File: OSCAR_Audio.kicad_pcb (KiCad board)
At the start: 2 copper layers, 91 x 87.1 mm, 125 parts, among them J1 InL, J2 InR, J3 OutR, J4 OutL, J5 SAI, J6 Vol, J7 +12V, J8 +12V, J9 ByPass, K1 G6K-2F-Y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

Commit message: Fix typo OPA1612 -> OPA1642. Note: an OPA with FET inputs is necessary here.
/!\  An OPA with FET inputs is necessary here.
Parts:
- U1: value OPA1612 -> OPA1642
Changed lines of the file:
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@@
 			)
 		)
-		(property "Value" "OPA1612"
-			(at -1.4525 4.085 0)
+		(property "Value" "OPA1642"
+			(at -1.2825 4.845 0)
 			(layer "B.SilkS")
 			(effects

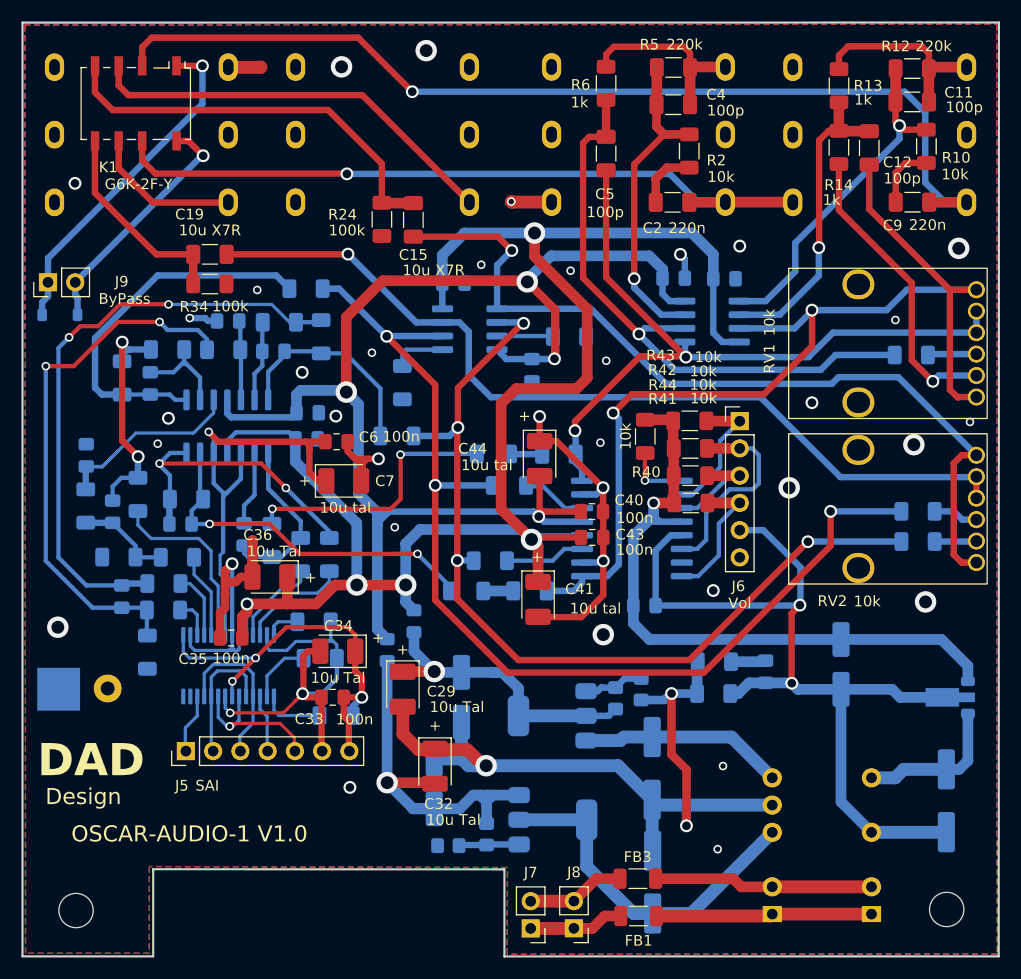
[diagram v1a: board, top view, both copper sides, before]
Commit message: Invert output summing stage to maintain correct phase
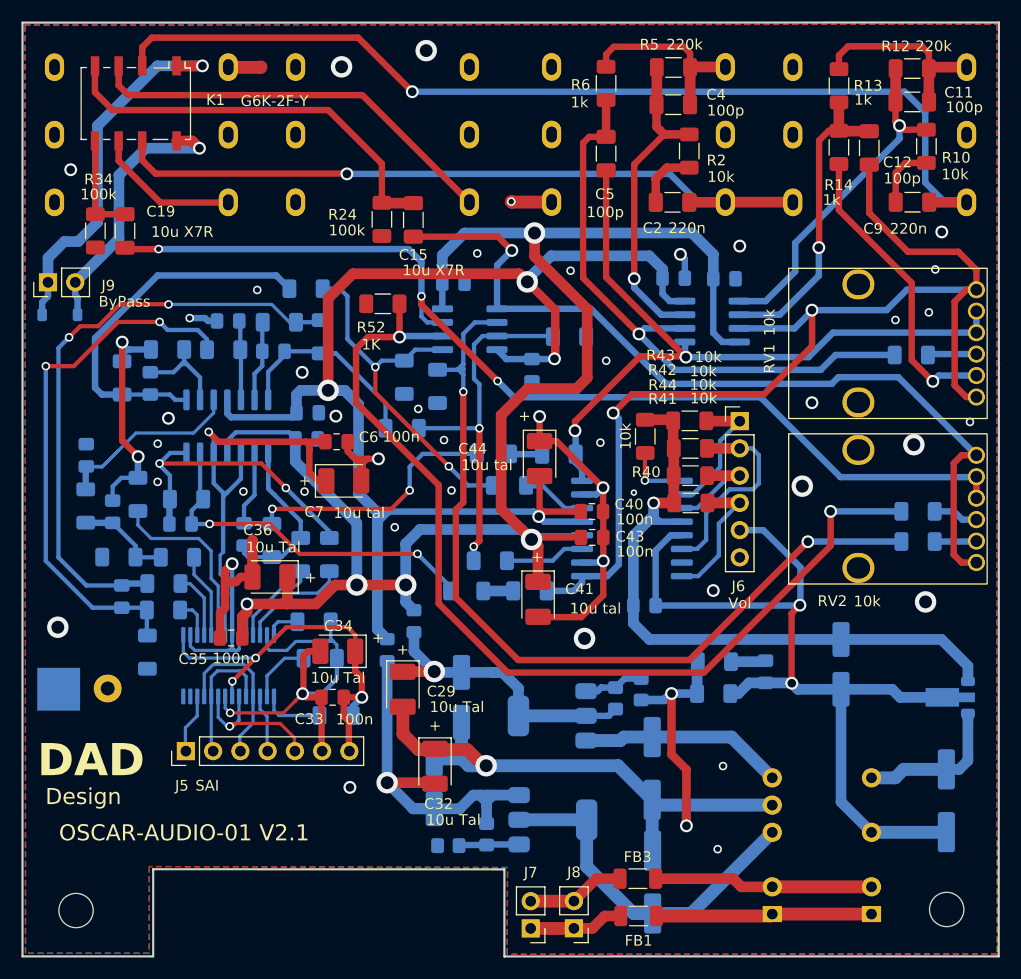
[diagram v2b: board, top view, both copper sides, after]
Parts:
- added R51: 1k, Resistor_SMD:R_1206_3216Metric_Pad1.30x1.75mm_HandSolder, B.Cu at (151.3, 79.2)
- added R52: 1K, Resistor_SMD:R_1206_3216Metric_Pad1.30x1.75mm_HandSolder, F.Cu at (146.2, 71.5)
- R18, R29: value 1k -> 100
- R25, R36: value 470 -> Option
- moved R34 11.8 mm to (119.4, 64.7), turned to -90 degrees
- moved C19 8.21 mm to (122.2, 64.7), turned to -90 degrees
- moved R19 0.87 mm to (148.0, 83.1)
- moved R36 0.53 mm to (148.2, 78.3)
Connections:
- R19 pad 2: Net-(U4A--) -> Net-(U4A-+)
- R22 pad 2: Net-(U4A--) -> Net-(U4A-+)
- R30 pad 2: Net-(U4B--) -> Net-(U4B-+)
- R33 pad 2: Net-(U4B--) -> Net-(U4B-+)
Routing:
- net Net-(U4B-+): track 5.07 -> 34.2 mm, vias 0 -> 2
- net Net-(U4A-+): track 5.24 -> 34.0 mm, vias 0 -> 2
- net Net-(C19-Pad2): track 82.9 -> 96.7 mm, vias 1 -> 3
- net Net-(C19-Pad1): track 19.1 -> 9.60 mm
- net Net-(U4B--): track 99.2 -> 92.5 mm, vias 3 -> 2
- net Net-(U4A--): track 85.3 -> 81.0 mm, vias 4 -> 2
- net /Analog/+R5V: track 31.8 -> 35.0 mm
- net /Analog/R0V: track 23.0 -> 25.7 mm
- net Net-(U5B-AINR): track 99.9 -> 101.9 mm
- net Net-(U2A--): track 34.6 -> 33.5 mm
- net Net-(C13-Pad2): track 20.0 -> 18.9 mm
- net +5VA: track 161.7 -> 161.1 mm
- net GNDA: vias 39 -> 47
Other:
- board text added: "OSCAR-AUDIO-01 V2.1"
- board text added: "Option"
- board text removed: "OSCAR-AUDIO-1 V1.0"

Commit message: Define R25 and R36 to 1k
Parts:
- R25: value Option -> 1K
- R36: value Option -> 1k
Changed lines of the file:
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@@
 			)
 		)
-		(property "Value" "Option"
+		(property "Value" "1K"
 			(at -0.1 -2.06 0)
 			(layer "B.SilkS")
@@
 			)
 		)
-		(property "Value" "Option"
+		(property "Value" "1k"
 			(at 2.15 3.7 0)
 			(layer "B.SilkS")
